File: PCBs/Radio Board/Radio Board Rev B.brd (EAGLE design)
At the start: 95.9 x 90.2 mm, 14 parts, among them J1 MOLEX_504050-0491

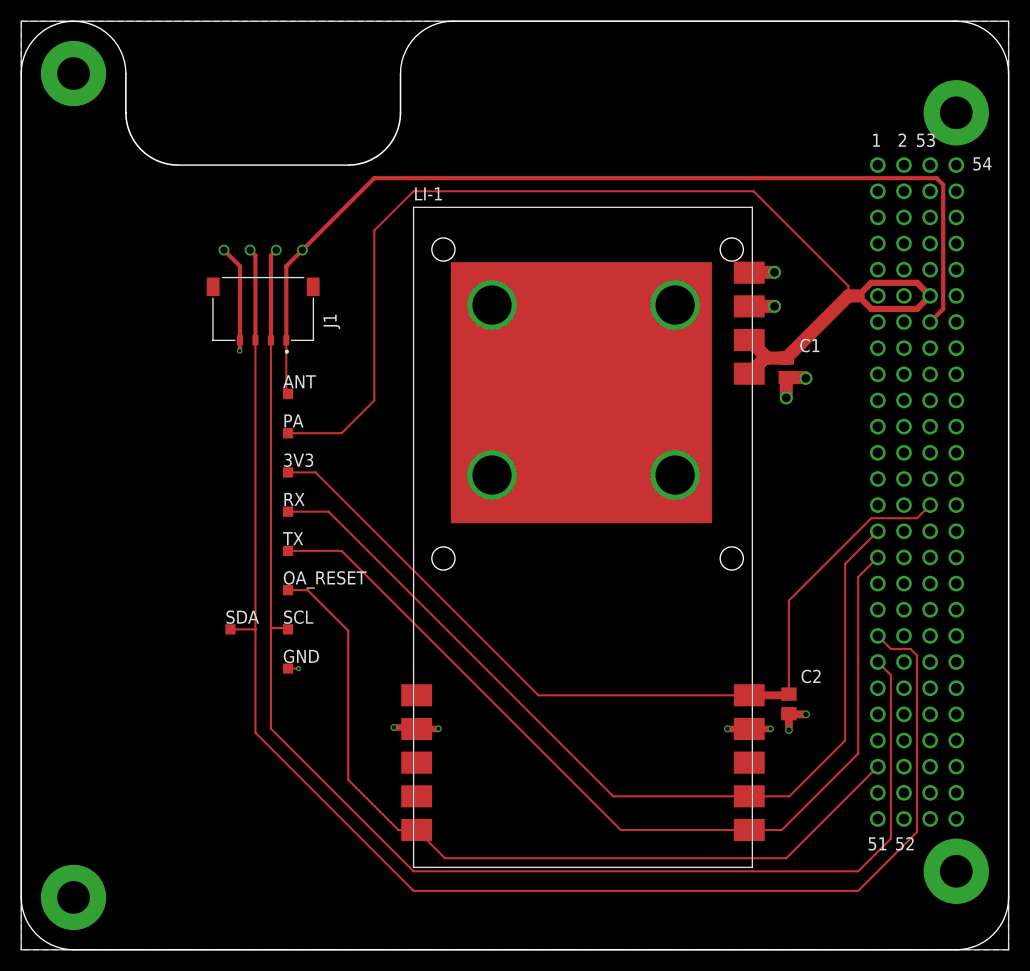
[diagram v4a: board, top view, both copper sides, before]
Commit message: Remove trace stubs
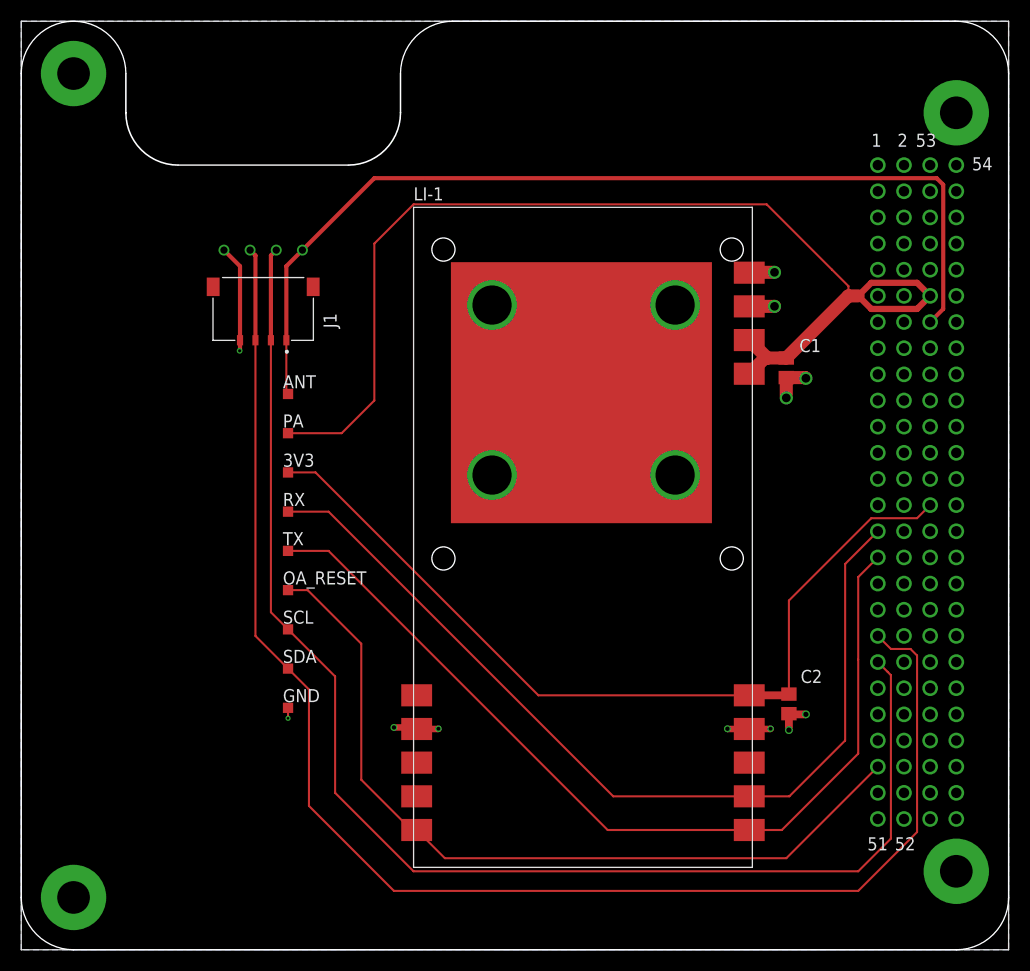
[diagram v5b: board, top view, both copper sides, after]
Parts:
- moved SDA 6.76 mm to (25.9, 27.3)
- moved GND 3.81 mm to (25.9, 23.5)
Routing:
- net SW3: track 110.8 -> 109.0 mm
- net SCL_ANT: track 133.3 -> 131.6 mm
- net SDA_ANT: track 144.2 -> 142.9 mm
- net OA_RESET: track 80.2 -> 79.5 mm
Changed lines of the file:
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@@
 <attribute name="TP_SIGNAL_NAME" value="" x="25.908" y="48.26" size="1" layer="37"/>
 </element>
-<element name="GND" library="testpad" library_urn="urn:adsk.eagle:library:385" package="TP10SQ" package3d_urn="urn:adsk.eagle:package:27962/1" value="TPTP10SQ" x="25.908" y="27.305" smashed="yes">
-<attribute name="NAME" x="25.4079" y="27.8549" size="1.27" layer="25"/>
-<attribute name="TP_SIGNAL_NAME" value="" x="25.908" y="25.4" size="1" layer="37"/>
+<element name="GND" library="testpad" library_urn="urn:adsk.eagle:library:385" package="TP10SQ" package3d_urn="urn:adsk.eagle:package:27962/1" value="TPTP10SQ" x="25.908" y="23.495" smashed="yes">
+<attribute name="NAME" x="25.4079" y="24.0449" size="1.27" layer="25"/>
+<attribute name="TP_SIGNAL_NAME" value="" x="25.908" y="21.59" size="1" layer="37"/>
 </element>
 <element name="J1" library="Molex 504050-0491" package="MOLEX_5040500491" value="MOLEX_504050-0491" x="23.495" y="62.23" smashed="yes" rot="R180">
@@
 <attribute name="PACKAGE" value="None" x="23.495" y="62.23" size="1.778" layer="27" rot="R180" display="off"/>
 </element>
-<element name="SDA" library="testpad" library_urn="urn:adsk.eagle:library:385" package="TP10SQ" package3d_urn="urn:adsk.eagle:package:27962/1" value="TPTP10SQ" x="20.32" y="31.115" smashed="yes">
-<attribute name="NAME" x="19.8199" y="31.6649" size="1.27" layer="25"/>
-<attribute name="TP_SIGNAL_NAME" value="" x="20.32" y="29.21" size="1" layer="37"/>
+<element name="SDA" library="testpad" library_urn="urn:adsk.eagle:library:385" package="TP10SQ" package3d_urn="urn:adsk.eagle:package:27962/1" value="TPTP10SQ" x="25.908" y="27.305" smashed="yes">
+<attribute name="NAME" x="25.4079" y="27.8549" size="1.27" layer="25"/>
+<attribute name="TP_SIGNAL_NAME" value="" x="25.908" y="25.4" size="1" layer="37"/>
 </element>
 <element name="SCL" library="testpad" library_urn="urn:adsk.eagle:library:385" package="TP10SQ" package3d_urn="urn:adsk.eagle:package:27962/1" value="TPTP10SQ" x="25.908" y="31.115" smashed="yes">
@@
 <contactref element="U$1" pad="100"/>
 <contactref element="GND" pad="TP"/>
-<wire x1="26.924" y1="27.305" x2="25.908" y2="27.305" width="0.2032" layer="1"/>
-<via x="26.924" y="27.305" extent="1-16" drill="0.254"/>
+<wire x1="25.908" y1="23.495" x2="25.908" y2="22.479" width="0.2032" layer="1"/>
+<via x="25.908" y="22.479" extent="1-16" drill="0.254"/>
 <contactref element="J1" pad="4"/>
 <wire x1="21.245" y1="59.19" x2="21.245" y2="66.385" width="0.4064" layer="1"/>
@@
 <wire x1="70.7" y1="55.94" x2="72.225" y2="57.465" width="1.27" layer="1"/>
 <wire x1="72.225" y1="57.465" x2="72.445" y2="57.465" width="1.27" layer="1"/>
-<wire x1="34.29" y1="69.85" x2="38.1" y2="73.66" width="0.2032" layer="1"/>
-<wire x1="34.29" y1="69.85" x2="34.29" y2="53.34" width="0.2032" layer="1"/>
+<wire x1="34.29" y1="68.58" x2="38.1" y2="72.39" width="0.2032" layer="1"/>
+<wire x1="34.29" y1="68.58" x2="34.29" y2="53.34" width="0.2032" layer="1"/>
 <wire x1="34.29" y1="53.34" x2="31.115" y2="50.165" width="0.2032" layer="1"/>
 <wire x1="31.115" y1="50.165" x2="25.908" y2="50.165" width="0.2032" layer="1"/>
-<wire x1="71.12" y1="73.66" x2="78.74" y2="66.04" width="0.2032" layer="1"/>
-<wire x1="38.1" y1="73.66" x2="71.12" y2="73.66" width="0.2032" layer="1"/>
+<wire x1="72.39" y1="72.39" x2="78.74" y2="66.04" width="0.2032" layer="1"/>
+<wire x1="38.1" y1="72.39" x2="72.39" y2="72.39" width="0.2032" layer="1"/>
 <wire x1="74.295" y1="57.465" x2="80.33" y2="63.5" width="1.27" layer="1"/>
 <wire x1="80.33" y1="63.5" x2="81.28" y2="63.5" width="1.27" layer="1"/>
@@
 <contactref element="OA_RESET" pad="TP"/>
 <wire x1="74.295" y1="8.89" x2="83.185" y2="17.78" width="0.2032" layer="1"/>
-<wire x1="27.813" y1="34.925" x2="31.75" y2="30.988" width="0.2032" layer="1"/>
+<wire x1="27.813" y1="34.925" x2="33.02" y2="29.718" width="0.2032" layer="1"/>
 <wire x1="27.813" y1="34.925" x2="25.908" y2="34.925" width="0.2032" layer="1"/>
 <wire x1="38.4" y1="11.63" x2="41.14" y2="8.89" width="0.2032" layer="1"/>
-<wire x1="36.63" y1="11.63" x2="38.4" y2="11.63" width="0.2032" layer="1"/>
-<wire x1="31.75" y1="30.988" x2="31.75" y2="16.51" width="0.2032" layer="1"/>
-<wire x1="31.75" y1="16.51" x2="36.63" y2="11.63" width="0.2032" layer="1"/>
+<wire x1="37.9" y1="11.63" x2="38.4" y2="11.63" width="0.2032" layer="1"/>
+<wire x1="33.02" y1="29.718" x2="33.02" y2="16.51" width="0.2032" layer="1"/>
+<wire x1="33.02" y1="16.51" x2="37.9" y2="11.63" width="0.2032" layer="1"/>
 </signal>
 <signal name="LI_TX">
@@
 <wire x1="81.28" y1="19.05" x2="73.86" y2="11.63" width="0.2032" layer="1"/>
 <wire x1="73.86" y1="11.63" x2="70.7" y2="11.63" width="0.2032" layer="1"/>
-<wire x1="70.7" y1="11.63" x2="58.22" y2="11.63" width="0.2032" layer="1"/>
-<wire x1="31.115" y1="38.735" x2="25.908" y2="38.735" width="0.2032" layer="1"/>
-<wire x1="58.22" y1="11.63" x2="31.115" y2="38.735" width="0.2032" layer="1"/>
+<wire x1="70.7" y1="11.63" x2="56.95" y2="11.63" width="0.2032" layer="1"/>
+<wire x1="29.845" y1="38.735" x2="25.908" y2="38.735" width="0.2032" layer="1"/>
+<wire x1="56.95" y1="11.63" x2="29.845" y2="38.735" width="0.2032" layer="1"/>
 </signal>
 <signal name="SW5">
@@
 <wire x1="83.185" y1="27.94" x2="84.1375" y2="26.9875" width="0.2032" layer="1"/>
 <wire x1="84.1375" y1="26.9875" x2="84.455" y2="26.67" width="0.2032" layer="1"/>
-<wire x1="24.245" y1="59.19" x2="24.245" y2="31.75" width="0.2032" layer="1"/>
-<wire x1="24.245" y1="31.75" x2="24.245" y2="31.242" width="0.2032" layer="1"/>
-<wire x1="24.245" y1="31.242" x2="24.245" y2="30.48" width="0.2032" layer="1"/>
-<wire x1="24.245" y1="30.48" x2="24.245" y2="21.475" width="0.2032" layer="1"/>
-<wire x1="38.1" y1="7.62" x2="24.245" y2="21.475" width="0.2032" layer="1"/>
-<wire x1="25.908" y1="31.115" x2="25.781" y2="31.242" width="0.2032" layer="1"/>
-<wire x1="25.781" y1="31.242" x2="24.245" y2="31.242" width="0.2032" layer="1"/>
 <wire x1="84.455" y1="26.67" x2="84.455" y2="10.795" width="0.2032" layer="1"/>
 <wire x1="84.455" y1="10.795" x2="81.28" y2="7.62" width="0.2032" layer="1"/>
-<wire x1="81.28" y1="7.62" x2="38.1" y2="7.62" width="0.2032" layer="1"/>
+<wire x1="38.1" y1="7.62" x2="81.28" y2="7.62" width="0.2032" layer="1"/>
+<wire x1="24.245" y1="59.19" x2="24.245" y2="32.778" width="0.2032" layer="1"/>
+<wire x1="24.245" y1="32.778" x2="25.908" y2="31.115" width="0.2032" layer="1"/>
+<wire x1="25.908" y1="31.115" x2="30.48" y2="26.543" width="0.2032" layer="1"/>
+<wire x1="30.48" y1="15.24" x2="38.1" y2="7.62" width="0.2032" layer="1"/>
+<wire x1="30.48" y1="26.543" x2="30.48" y2="15.24" width="0.2032" layer="1"/>
 </signal>
 <signal name="SDA_ANT">
@@
 <via x="22.225" y="67.945" extent="1-16" drill="0.7112"/>
 <contactref element="SDA" pad="TP"/>
-<wire x1="22.745" y1="31.115" x2="22.745" y2="21.07" width="0.2032" layer="1"/>
-<wire x1="22.745" y1="21.07" x2="38.1" y2="5.715" width="0.2032" layer="1"/>
-<wire x1="22.745" y1="31.115" x2="20.32" y2="31.115" width="0.2032" layer="1"/>
 <wire x1="81.28" y1="5.715" x2="86.995" y2="11.43" width="0.2032" layer="1"/>
 <wire x1="86.995" y1="28.575" x2="86.36" y2="29.21" width="0.2032" layer="1"/>
-<wire x1="38.1" y1="5.715" x2="81.28" y2="5.715" width="0.2032" layer="1"/>
 <wire x1="86.995" y1="11.43" x2="86.995" y2="28.575" width="0.2032" layer="1"/>
 <wire x1="84.455" y1="29.21" x2="86.36" y2="29.21" width="0.2032" layer="1"/>
 <contactref element="U$1" pad="37"/>
 <wire x1="83.185" y1="30.48" x2="84.455" y2="29.21" width="0.2032" layer="1"/>
-<wire x1="22.745" y1="59.19" x2="22.745" y2="31.115" width="0.2032" layer="1"/>
+<wire x1="25.908" y1="27.305" x2="27.94" y2="25.273" width="0.2032" layer="1"/>
+<wire x1="27.94" y1="25.273" x2="27.94" y2="13.97" width="0.2032" layer="1"/>
+<wire x1="27.94" y1="13.97" x2="36.195" y2="5.715" width="0.2032" layer="1"/>
+<wire x1="36.195" y1="5.715" x2="81.28" y2="5.715" width="0.2032" layer="1"/>
+<wire x1="22.745" y1="30.468" x2="25.908" y2="27.305" width="0.2032" layer="1"/>
+<wire x1="22.745" y1="59.19" x2="22.745" y2="30.468" width="0.2032" layer="1"/>
 </signal>
 </signals>
